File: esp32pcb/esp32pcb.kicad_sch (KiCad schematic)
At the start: 27 parts, among them J1 Conn_01x04, J2 Screw_Terminal_01x03, J3 Screw_Terminal_01x08, J4 Screw_Terminal_01x02, J5 USB_C_Receptacle_USB2.0_16P, K1 RT314A05, Q1 UMH3N, Q2 BC817, SW1 SW_SPST, U1 ESP32-WROOM-32D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

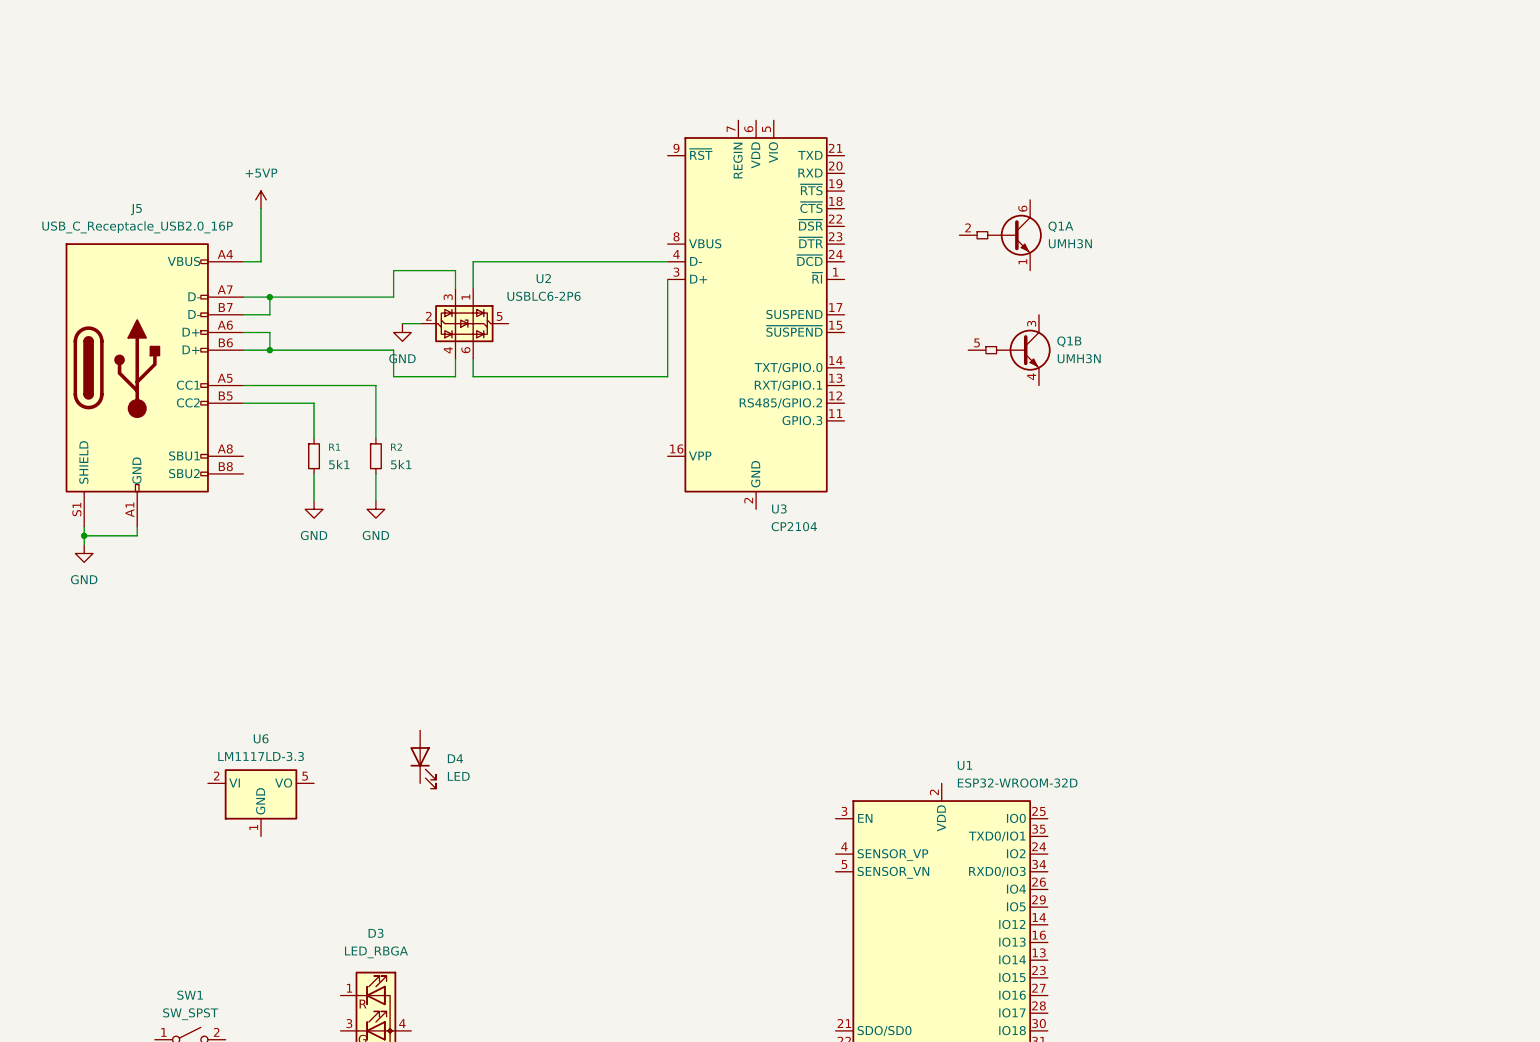
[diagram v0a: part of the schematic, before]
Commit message: wiring, connections between cp2104 and the usb c receptacle and stuffs
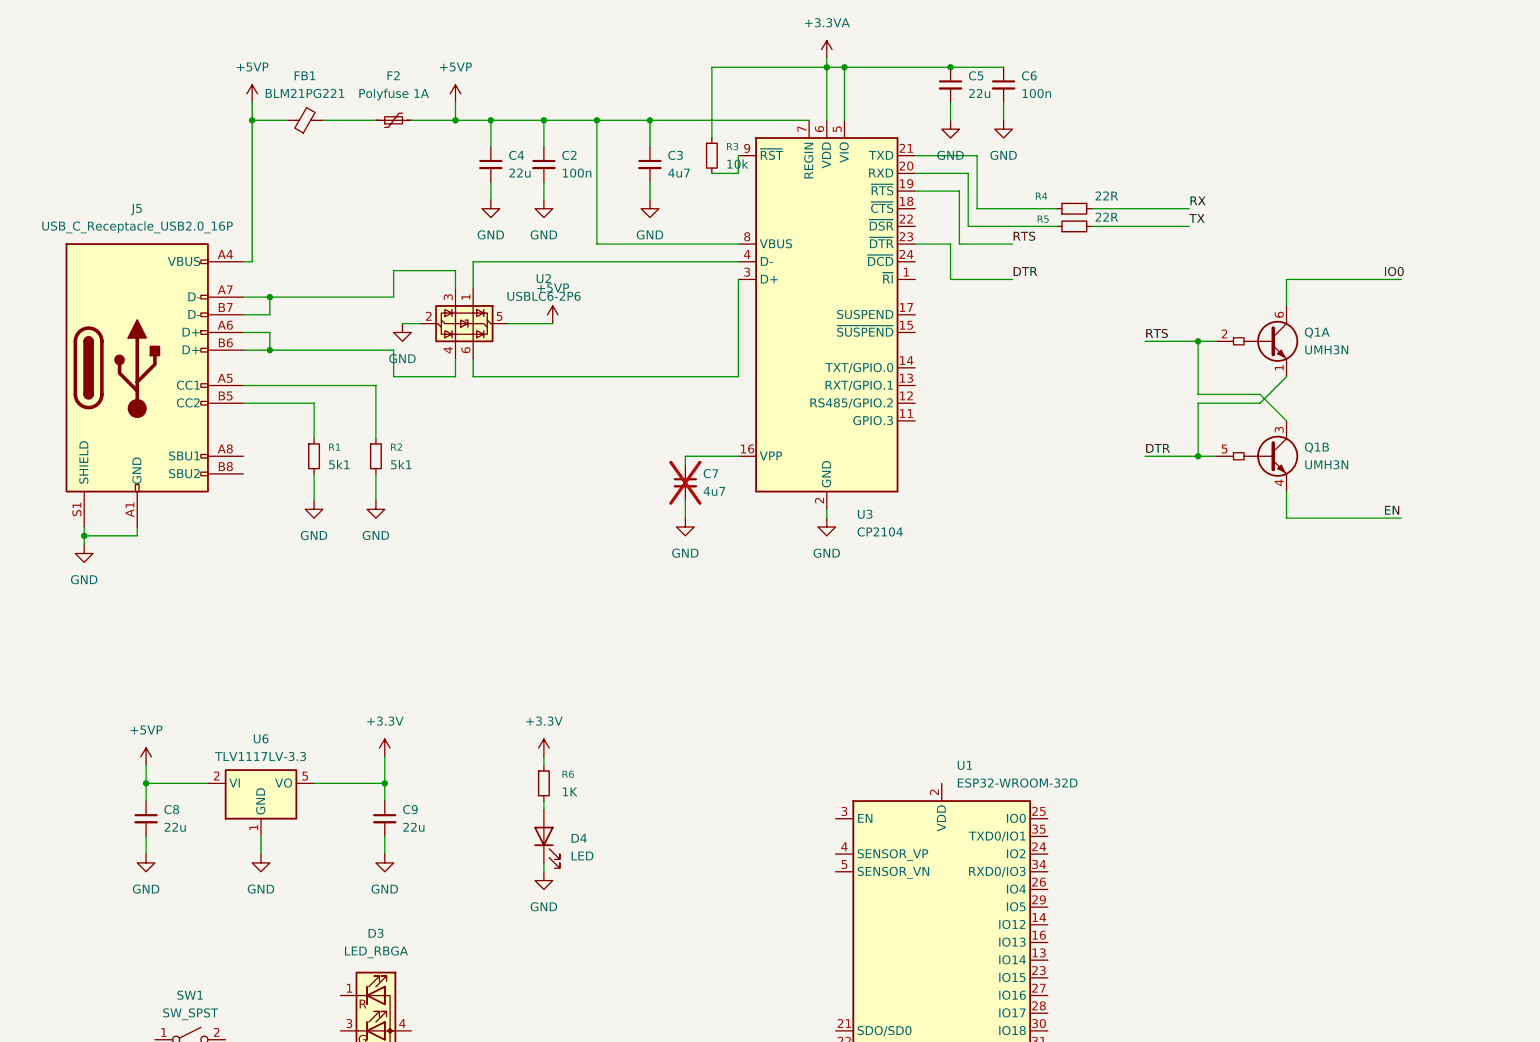
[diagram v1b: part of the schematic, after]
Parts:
- added C2, C6: 100n, symbol Device:C_Small
- added C3, C7: 4u7, symbol Device:C_Small
- added C4, C5, C8, C9: 22u, symbol Device:C_Small
- added F2: Polyfuse 1A, symbol Device:Polyfuse_Small
- added FB1: BLM21PG221, symbol Device:FerriteBead_Small
- added R3: 10k, symbol Device:R_Small
- added R4, R5: 22R, symbol Device:R_Small
- added R6: 1K, symbol Device:R_Small
- U6: value LM1117LD-3.3 -> TLV1117LV-3.3
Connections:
- net +5VP: now also U2.5 (VBUS), U3.7 (REGIN), U3.8 (VBUS), U6.2 (VI), U6.3 (VI), U6.4 (VI), C2.1, C3.1, C4.1, C8.1, F2.2, FB1.1
- net GND: now also D4.1 (K), U3.2 (GND), U3.25 (GND), U6.1 (GND), C2.2, C3.2, C4.2, C5.2, C6.2, C7.2, C8.2, C9.2
- net at D4.2 (A): now also R6.2
- net +3.3V: now reaches U6.5 (VO), U6.6 (VO), U6.7 (VO), U6.9 (VO)
- net +3.3V: now also C9.1, R6.1
- net at U3.16 (VPP): now also C7.1
- net RTS: now reaches U3.19 (~{RTS})
- net RTS: now also Q1.2 (B1), Q1.3 (C2)
- net at U3.20 (RXD): now also R5.1
- net at U3.21 (TXD): now also R4.1
- net DTR: now reaches U3.23 (~{DTR})
- net DTR: now also Q1.1 (E1), Q1.5 (B2)
- net +3.3VA: now reaches U3.5 (VIO)
- net +3.3VA: now also U3.6 (VDD), C5.1, C6.1, R3.1
- net at U3.9 (~{RST}): now also R3.2
- net IO0: now reaches Q1.6 (C1)
- net EN: now reaches Q1.4 (E2)
- new net: F2.1, FB1.2
- new net RX: R4.2
- new net TX: R5.2
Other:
- moved on the sheet: D4, Q1A, Q1B, U3
